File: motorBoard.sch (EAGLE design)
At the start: 73 parts

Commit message: Mostly done with the small board
Removed 1 motor channel, all 3V3 encoders, level shifter enable switches, 1 gpio header. Moved around a ton of components.
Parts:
- removed 1_ENCD3V3, 1_ENCD5V, 2_ENCD3V3, 3_ENCD3V3, 4_ENCD3V3: MOLEX5, HuskyRobotics2017-18:MOLEX5
- removed BASIC_HEADER1: 6BASIC_HEADER, HuskyRobotics2017-18:6BASIC_HEADER
- removed C9: 0.1uF, eagle-ltspice:CC1206
- removed LIMITA1, LIMITB1, POT1, PWM1: MOLEX3, HuskyRobotics2017-18:MOLEX3
- removed R10, R11, R8, R9: 4.7k, eagle-ltspice:RR1206
- removed SHIFT1: LEVEL-SHIFTER_NVT2003DPNVT_2003DP_LEVEL_SHIFTER, HuskyRobotics2017-18:LEVEL-SHIFTER_NVT2003DPNVT_2003DP_LEVEL_SHIFTER
- removed SHIFT_EN: SMD4SWSMD4SW, HuskyRobotics2017-18:SMD4SWSMD4SW
- U$1: value OOPS_SPACE -> OOPS_SPACESMALL; device HuskyRobotics2017-18:OOPS_SPACE -> HuskyRobotics2017-18:OOPS_SPACESMALL
- renumbered U$2 to BUTTON
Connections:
- removed net BASIC_HEADER1-1: BASIC_HEADER1.1, PSOC4200L.P4.1
- removed net BASIC_HEADER1-2: BASIC_HEADER1.2, PSOC4200L.P4.2
- removed net BASIC_HEADER1-3: BASIC_HEADER1.3, PSOC4200L.P4.3
- removed net BASIC_HEADER1-6: BASIC_HEADER1.6, PSOC4200L.P4.6
- removed net LEVEL_SHIFT_EN1: R11.2, SHIFT1.EN, SHIFT_EN.1B
- removed net LEVEL_SHIFT_EN2: R10.2, SHIFT2.EN, SHIFT_EN.2B
- removed net LEVEL_SHIFT_EN3: R9.2, SHIFT3.EN, SHIFT_EN.3B
- removed net LEVEL_SHIFT_EN4: R8.2, SHIFT4.EN, SHIFT_EN.4B
- removed net MOTOR1A1: 1_ENCD3V3.4, PSOC4200L.P0.2, SHIFT1.A1
- removed net MOTOR1A2: 1_ENCD3V3.3, PSOC4200L.P0.1, SHIFT1.A2
- removed net MOTOR1A3: 1_ENCD3V3.2, PSOC4200L.P0.0, SHIFT1.A3
- removed net MOTOR1B1: 1_ENCD5V.4, SHIFT1.B1
- removed net MOTOR1B2: 1_ENCD5V.3, SHIFT1.B2
- removed net MOTOR1B3: 1_ENCD5V.2, SHIFT1.B3
- removed net MOTOR1LIMA: LIMITA1.2, PSOC4200L.P0.3
- removed net MOTOR1LIMB: LIMITB1.2, PSOC4200L.P0.4
- removed net MOTOR1POT: POT1.2, PSOC4200L.P0.7
- removed net MOTOR1PWM: PSOC4200L.P0.5, PWM1.2
- net +3V3: no longer 1_ENCD3V3.1, 2_ENCD3V3.1, 3_ENCD3V3.1, 4_ENCD3V3.1, LIMITA1.1, LIMITB1.1, PWM1.1, SHIFT1.AREF, SHIFT_EN.1A, SHIFT_EN.2A, SHIFT_EN.3A, SHIFT_EN.4A
- net +5V: now also SHIFT2.EN, SHIFT3.EN, SHIFT4.EN; no longer 1_ENCD5V.1, C9.2, POT1.1, SHIFT1.BREF
- net BASIC_HEADER1-4: no longer BASIC_HEADER1.4
- net BASIC_HEADER1-5: no longer BASIC_HEADER1.5
- net CLK_EXT: no longer PSOC4200L.P0.6
- net GNDA: no longer 1_ENCD3V3.5, 1_ENCD5V.5, 2_ENCD3V3.5, 3_ENCD3V3.5, 4_ENCD3V3.5, C9.1, LIMITA1.3, LIMITB1.3, POT1.3, PWM1.3, R10.1, R11.1, R8.1, R9.1, SHIFT1.GND
- net LED4: now also PSOC4200L.P4.3; no longer PSOC4200L.VBUS/P13.2
- net LED5: now also PSOC4200L.P4.2; no longer PSOC4200L.D+/P13.0
- net LED7: now also PSOC4200L.P4.1; no longer PSOC4200L.D-/P13.1
- net MOTOR2A1: no longer 2_ENCD3V3.4
- net MOTOR2A2: no longer 2_ENCD3V3.3
- net MOTOR2A3: no longer 2_ENCD3V3.2
- net MOTOR3A1: no longer 3_ENCD3V3.4
- net MOTOR3A2: no longer 3_ENCD3V3.3
- net MOTOR3A3: no longer 3_ENCD3V3.2
- net MOTOR4A1: no longer 4_ENCD3V3.4
- net MOTOR4A2: no longer 4_ENCD3V3.3
- net MOTOR4A3: no longer 4_ENCD3V3.2
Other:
- note removed: "Motor1"

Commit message: "Done" except for silk screen and DFM check
Added 24V terminal blocks, second CAN header, limit switch debounces.
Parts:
- added C14, C15, C16, C17, C3, C9: 0.1uF, eagle-ltspice:CC1206
- added CAN1: 22-23-2021, con-molex:22-23-2021
- added J1, J2: TE-TERM-BLOCK, HuskyRobotics17-18:TE-TERM-BLOCK
- added R10, R11, R14, R15, R8, R9: 1k, eagle-ltspice:RR1206
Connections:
- net +24V: now also J1.1, J2.1
- net +3V3: now also C14.2, C15.2, C16.1, C17.1, C3.2, C9.2
- net CANH: now also CAN1-1.S
- net CANL: now also CAN1-2.S
- net GNDA: now also J1.2, J2.2, R10.1, R11.1, R14.1, R15.1, R8.1, R9.1
- net MOTOR2LIMA: now also C17.2, R14.2
- net MOTOR2LIMB: now also C16.2, R15.2
- net MOTOR3LIMA: now also C14.1, R11.2
- net MOTOR3LIMB: now also C15.1, R10.2
- net MOTOR4LIMA: now also C9.1, R9.2
- net MOTOR4LIMB: now also C3.1, R8.2
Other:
- note removed: "Power connector?"
- moved on the sheet: 3.3V_DC-DC, 5V_DC-DC, C4, C5

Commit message: Finished Silk Screening
Ready for DFM test!
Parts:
- removed 6: (no value), eagle-ltspice:LED_E
- removed LIMITA4, LIMITB4, POT4, PWM4: MOLEX3, HuskyRobotics2017-18:MOLEX3
- added 1: (no value), eagle-ltspice:LED_E
- added LIMITA1, LIMITB1, POT1, PWM1: MOLEX3, HuskyRobotics2017-18:MOLEX3
- renumbered 2_ENCD5V to ENCD1, 3_ENCD5V to ENCD2, 4_ENCD5V to ENCD3, 5 to 2, 7 to 3, OSC to OSC_EXT
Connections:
- net +3V3: now also LIMITA1.1, LIMITB1.1, PWM1.1; no longer LIMITA4.1, LIMITB4.1, PWM4.1
- net +5V: now also POT1.1; no longer POT4.1
- net GNDA: now also LIMITA1.3, LIMITB1.3, POT1.3, PWM1.3; no longer LIMITA4.3, LIMITB4.3, POT4.3, PWM4.3
- net LED4: now also 1.A; no longer 4.A
- net LED6: now also 4.A; no longer 6.A
- net MOTOR2LIMA: now also LIMITA1.2; no longer LIMITA2.2
- net MOTOR2LIMB: now also LIMITB1.2; no longer LIMITB2.2
- net MOTOR2POT: now also POT1.2; no longer POT2.2
- net MOTOR2PWM: now also PWM1.2; no longer PWM2.2
- net MOTOR3LIMA: now also LIMITA2.2; no longer LIMITA3.2
- net MOTOR3LIMB: now also LIMITB2.2; no longer LIMITB3.2
- net MOTOR3POT: now also POT2.2; no longer POT3.2
- net MOTOR3PWM: now also PWM2.2; no longer PWM3.2
- net MOTOR4LIMA: now also LIMITA3.2; no longer LIMITA4.2
- net MOTOR4LIMB: now also LIMITB3.2; no longer LIMITB4.2
- net MOTOR4POT4: now also POT3.2; no longer POT4.2
- net MOTOR4PWM: now also PWM3.2; no longer PWM4.2
- net N$10: now also 1.C; no longer 4.C
- net N$17: now also 4.C; no longer 6.C
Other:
- moved on the sheet: 4, LIMITA2, LIMITA3, LIMITB2, LIMITB3, POT2, POT3, PWM2, PWM3

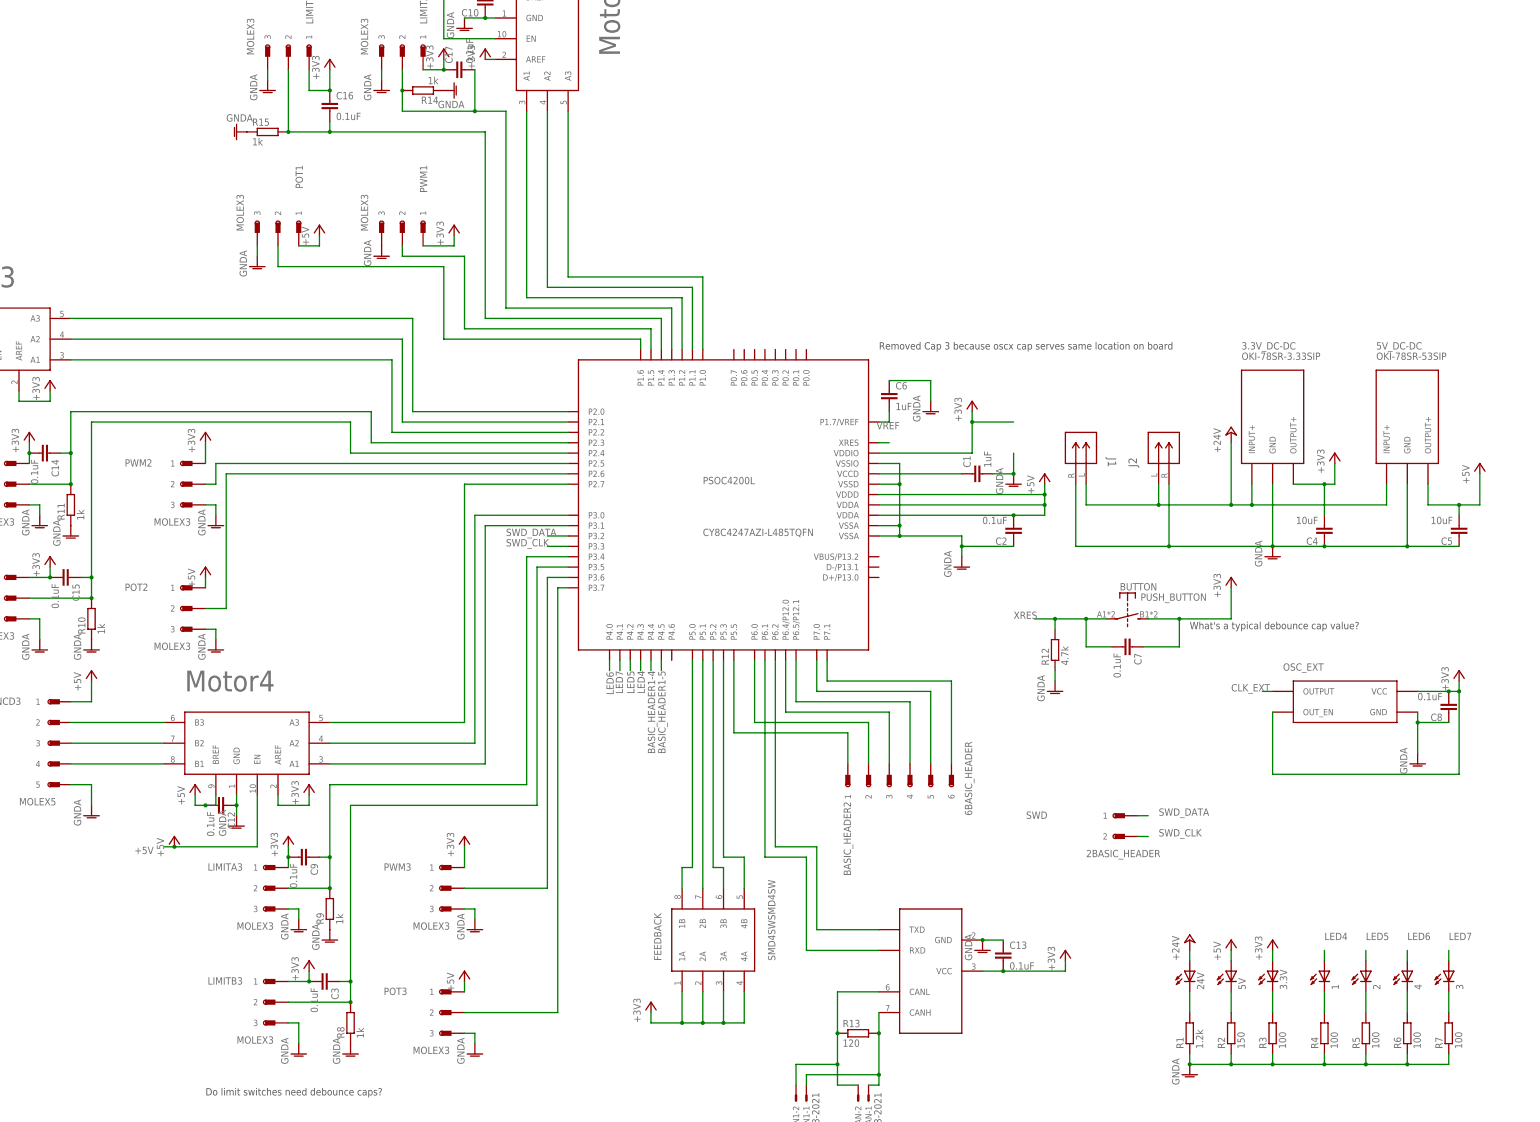
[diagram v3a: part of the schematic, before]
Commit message: Changed Resistor Values
Now match that of order
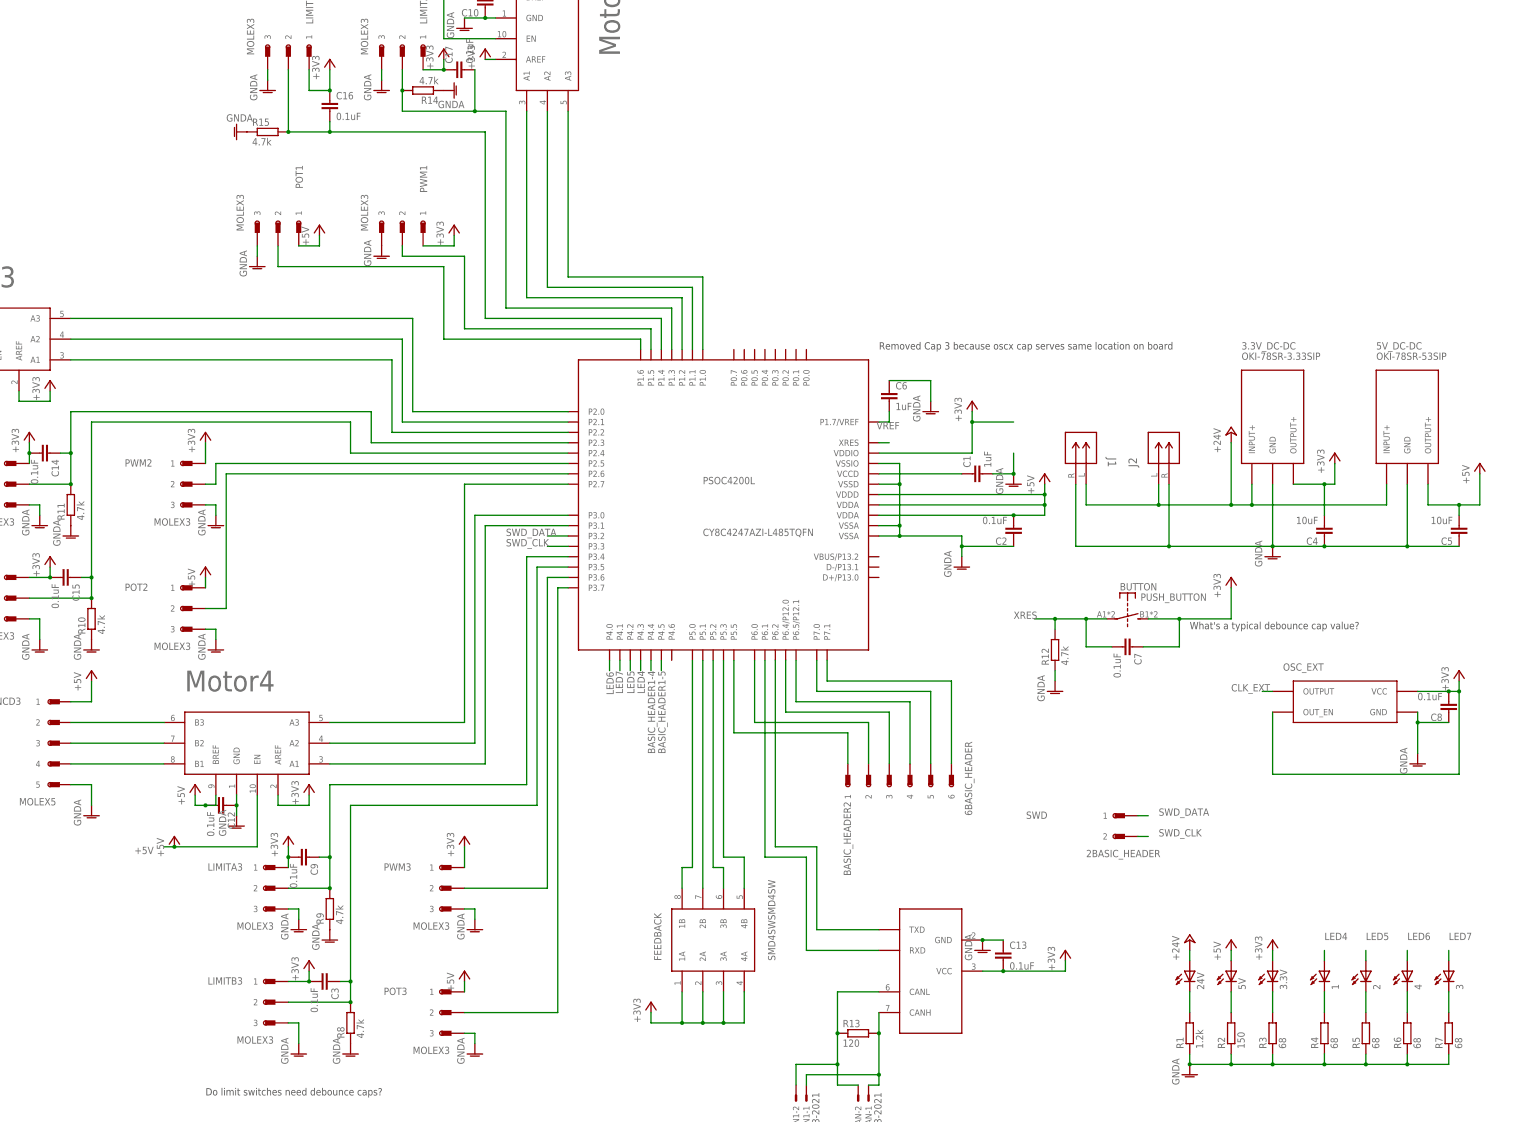
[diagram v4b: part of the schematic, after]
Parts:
- R10, R11, R14, R15, R8, R9: value 1k -> 4.7k
- R3, R4, R5, R6, R7: value 100 -> 68
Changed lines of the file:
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@@
 <part name="R2" library="eagle-ltspice" library_urn="urn:adsk.eagle:library:217" deviceset="R" device="R1206" package3d_urn="urn:adsk.eagle:package:13301/1" value="150"/>
 <part name="3.3V" library="eagle-ltspice" library_urn="urn:adsk.eagle:library:217" deviceset="LED_E" device="" package3d_urn="urn:adsk.eagle:package:13319/1"/>
-<part name="R3" library="eagle-ltspice" library_urn="urn:adsk.eagle:library:217" deviceset="R" device="R1206" package3d_urn="urn:adsk.eagle:package:13301/1" value="100"/>
+<part name="R3" library="eagle-ltspice" library_urn="urn:adsk.eagle:library:217" deviceset="R" device="R1206" package3d_urn="urn:adsk.eagle:package:13301/1" value="68"/>
 <part name="1" library="eagle-ltspice" library_urn="urn:adsk.eagle:library:217" deviceset="LED_E" device="" package3d_urn="urn:adsk.eagle:package:13319/1"/>
-<part name="R4" library="eagle-ltspice" library_urn="urn:adsk.eagle:library:217" deviceset="R" device="R1206" package3d_urn="urn:adsk.eagle:package:13301/1" value="100"/>
+<part name="R4" library="eagle-ltspice" library_urn="urn:adsk.eagle:library:217" deviceset="R" device="R1206" package3d_urn="urn:adsk.eagle:package:13301/1" value="68"/>
 <part name="2" library="eagle-ltspice" library_urn="urn:adsk.eagle:library:217" deviceset="LED_E" device="" package3d_urn="urn:adsk.eagle:package:13319/1"/>
-<part name="R5" library="eagle-ltspice" library_urn="urn:adsk.eagle:library:217" deviceset="R" device="R1206" package3d_urn="urn:adsk.eagle:package:13301/1" value="100"/>
+<part name="R5" library="eagle-ltspice" library_urn="urn:adsk.eagle:library:217" deviceset="R" device="R1206" package3d_urn="urn:adsk.eagle:package:13301/1" value="68"/>
 <part name="4" library="eagle-ltspice" library_urn="urn:adsk.eagle:library:217" deviceset="LED_E" device="" package3d_urn="urn:adsk.eagle:package:13319/1"/>
-<part name="R6" library="eagle-ltspice" library_urn="urn:adsk.eagle:library:217" deviceset="R" device="R1206" package3d_urn="urn:adsk.eagle:package:13301/1" value="100"/>
+<part name="R6" library="eagle-ltspice" library_urn="urn:adsk.eagle:library:217" deviceset="R" device="R1206" package3d_urn="urn:adsk.eagle:package:13301/1" value="68"/>
 <part name="3" library="eagle-ltspice" library_urn="urn:adsk.eagle:library:217" deviceset="LED_E" device="" package3d_urn="urn:adsk.eagle:package:13319/1"/>
-<part name="R7" library="eagle-ltspice" library_urn="urn:adsk.eagle:library:217" deviceset="R" device="R1206" package3d_urn="urn:adsk.eagle:package:13301/1" value="100"/>
+<part name="R7" library="eagle-ltspice" library_urn="urn:adsk.eagle:library:217" deviceset="R" device="R1206" package3d_urn="urn:adsk.eagle:package:13301/1" value="68"/>
 <part name="P+9" library="supply1" library_urn="urn:adsk.eagle:library:371" deviceset="+24V" device=""/>
 <part name="P+10" library="supply1" library_urn="urn:adsk.eagle:library:371" deviceset="+24V" device=""/>
@@
 <part name="J2" library="HuskyRobotics17-18" deviceset="TE-TERM-BLOCK" device=""/>
 <part name="CAN1" library="con-molex" library_urn="urn:adsk.eagle:library:165" deviceset="22-23-2021" device=""/>
-<part name="R8" library="eagle-ltspice" library_urn="urn:adsk.eagle:library:217" deviceset="R" device="R1206" package3d_urn="urn:adsk.eagle:package:13301/1" value="1k"/>
+<part name="R8" library="eagle-ltspice" library_urn="urn:adsk.eagle:library:217" deviceset="R" device="R1206" package3d_urn="urn:adsk.eagle:package:13301/1" value="4.7k"/>
 <part name="GND6" library="supply1" library_urn="urn:adsk.eagle:library:371" deviceset="GNDA" device=""/>
-<part name="R9" library="eagle-ltspice" library_urn="urn:adsk.eagle:library:217" deviceset="R" device="R1206" package3d_urn="urn:adsk.eagle:package:13301/1" value="1k"/>
+<part name="R9" library="eagle-ltspice" library_urn="urn:adsk.eagle:library:217" deviceset="R" device="R1206" package3d_urn="urn:adsk.eagle:package:13301/1" value="4.7k"/>
 <part name="GND12" library="supply1" library_urn="urn:adsk.eagle:library:371" deviceset="GNDA" device=""/>
-<part name="R10" library="eagle-ltspice" library_urn="urn:adsk.eagle:library:217" deviceset="R" device="R1206" package3d_urn="urn:adsk.eagle:package:13301/1" value="1k"/>
+<part name="R10" library="eagle-ltspice" library_urn="urn:adsk.eagle:library:217" deviceset="R" device="R1206" package3d_urn="urn:adsk.eagle:package:13301/1" value="4.7k"/>
 <part name="GND14" library="supply1" library_urn="urn:adsk.eagle:library:371" deviceset="GNDA" device=""/>
-<part name="R11" library="eagle-ltspice" library_urn="urn:adsk.eagle:library:217" deviceset="R" device="R1206" package3d_urn="urn:adsk.eagle:package:13301/1" value="1k"/>
+<part name="R11" library="eagle-ltspice" library_urn="urn:adsk.eagle:library:217" deviceset="R" device="R1206" package3d_urn="urn:adsk.eagle:package:13301/1" value="4.7k"/>
 <part name="GND15" library="supply1" library_urn="urn:adsk.eagle:library:371" deviceset="GNDA" device=""/>
-<part name="R14" library="eagle-ltspice" library_urn="urn:adsk.eagle:library:217" deviceset="R" device="R1206" package3d_urn="urn:adsk.eagle:package:13301/1" value="1k"/>
+<part name="R14" library="eagle-ltspice" library_urn="urn:adsk.eagle:library:217" deviceset="R" device="R1206" package3d_urn="urn:adsk.eagle:package:13301/1" value="4.7k"/>
 <part name="GND16" library="supply1" library_urn="urn:adsk.eagle:library:371" deviceset="GNDA" device=""/>
-<part name="R15" library="eagle-ltspice" library_urn="urn:adsk.eagle:library:217" deviceset="R" device="R1206" package3d_urn="urn:adsk.eagle:package:13301/1" value="1k"/>
+<part name="R15" library="eagle-ltspice" library_urn="urn:adsk.eagle:library:217" deviceset="R" device="R1206" package3d_urn="urn:adsk.eagle:package:13301/1" value="4.7k"/>
 <part name="GND17" library="supply1" library_urn="urn:adsk.eagle:library:371" deviceset="GNDA" device=""/>
 <part name="C3" library="eagle-ltspice" library_urn="urn:adsk.eagle:library:217" deviceset="C" device="C1206" package3d_urn="urn:adsk.eagle:package:13279/1" value="0.1uF"/>

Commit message: Cleaned Up Schematic
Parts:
- renumbered U$1 to PROTOTYPINGSPACE
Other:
- note removed: "Do limit switches need debounce caps?"
- note removed: "Need resistor Values!"
- note removed: "What's a typical debounce cap value?"
- moved on the sheet: 3.3V_DC-DC, 5V_DC-DC, BUTTON, C10, C11, C14, C15, C16, C17, C4, C5, C7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
